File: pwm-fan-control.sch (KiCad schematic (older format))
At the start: 19 parts, among them J1 Fan-out, J2 PWM and power, J4 Fan-out, Q1 Q_PMOS_GSD, Q2 Q_PMOS_GSD, U1 LM358

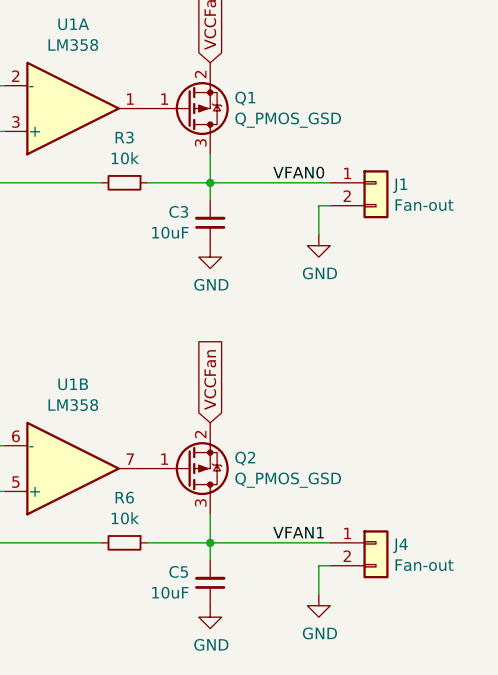
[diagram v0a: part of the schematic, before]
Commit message: improved bird, added silscreen to the back
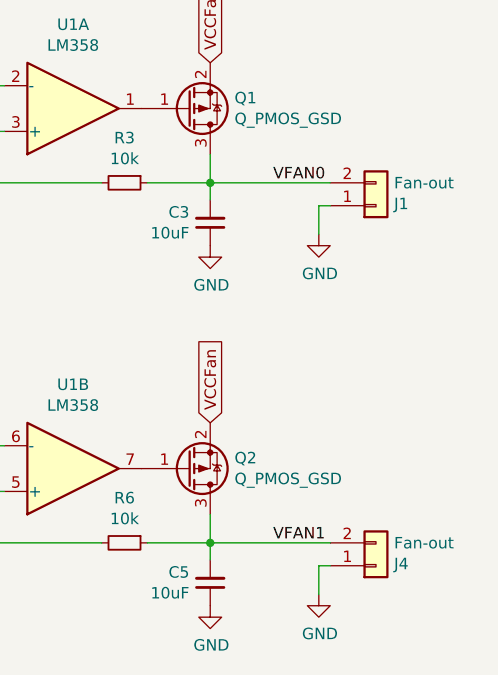
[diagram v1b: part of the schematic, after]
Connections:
- net GND: now also J1.1 (Pin_1), J4.1 (Pin_1); no longer J1.2 (Pin_2), J4.2 (Pin_2)
- net VFAN0: now also J1.2 (Pin_2); no longer J1.1 (Pin_1)
- net VFAN1: now also J4.2 (Pin_2); no longer J4.1 (Pin_1)
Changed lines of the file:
@@
 Date "2018-10-12"
 Rev "1"
-Comp "Design by N2"
+Comp "Design by N2: http://ee.david.promo"
 Comment1 "Schematic layout and PCB by Duckle"
 Comment2 ""
@@
 L Connector_Generic:Conn_01x02 J1
 U 1 1 5BC195AC
-P 6825 3775
-F 0 "J1" H 6904 3767 50  0000 L CNN
-F 1 "Fan-out" H 6904 3676 50  0000 L CNN
-F 2 "Connector_PinHeader_2.54mm:PinHeader_1x02_P2.54mm_Vertical" H 6825 3775 50  0001 C CNN
-F 3 "~" H 6825 3775 50  0001 C CNN
-	1    6825 3775
-	1    0    0    -1
+P 6825 3875
+F 0 "J1" H 6904 3867 50  0000 L CNN
+F 1 "Fan-out" H 6904 3776 50  0000 L CNN
+F 2 "Connector_PinHeader_2.54mm:PinHeader_1x02_P2.54mm_Vertical" H 6825 3875 50  0001 C CNN
+F 3 "~" H 6825 3875 50  0001 C CNN
+	1    6825 3875
+	1    0    0    1
 $EndComp
 Text Label 6375 3775 0    50   ~ 0
@@
 L Connector_Generic:Conn_01x02 J4
 U 1 1 5BC2F114
-P 6825 5350
-F 0 "J4" H 6904 5342 50  0000 L CNN
-F 1 "Fan-out" H 6904 5251 50  0000 L CNN
-F 2 "Connector_PinHeader_2.54mm:PinHeader_1x02_P2.54mm_Vertical" H 6825 5350 50  0001 C CNN
-F 3 "~" H 6825 5350 50  0001 C CNN
-	1    6825 5350
-	1    0    0    -1
+P 6825 5450
+F 0 "J4" H 6904 5442 50  0000 L CNN
+F 1 "Fan-out" H 6904 5351 50  0000 L CNN
+F 2 "Connector_PinHeader_2.54mm:PinHeader_1x02_P2.54mm_Vertical" H 6825 5450 50  0001 C CNN
+F 3 "~" H 6825 5450 50  0001 C CNN
+	1    6825 5450
+	1    0    0    1
 $EndComp
 Text Label 6375 5350 0    50   ~ 0

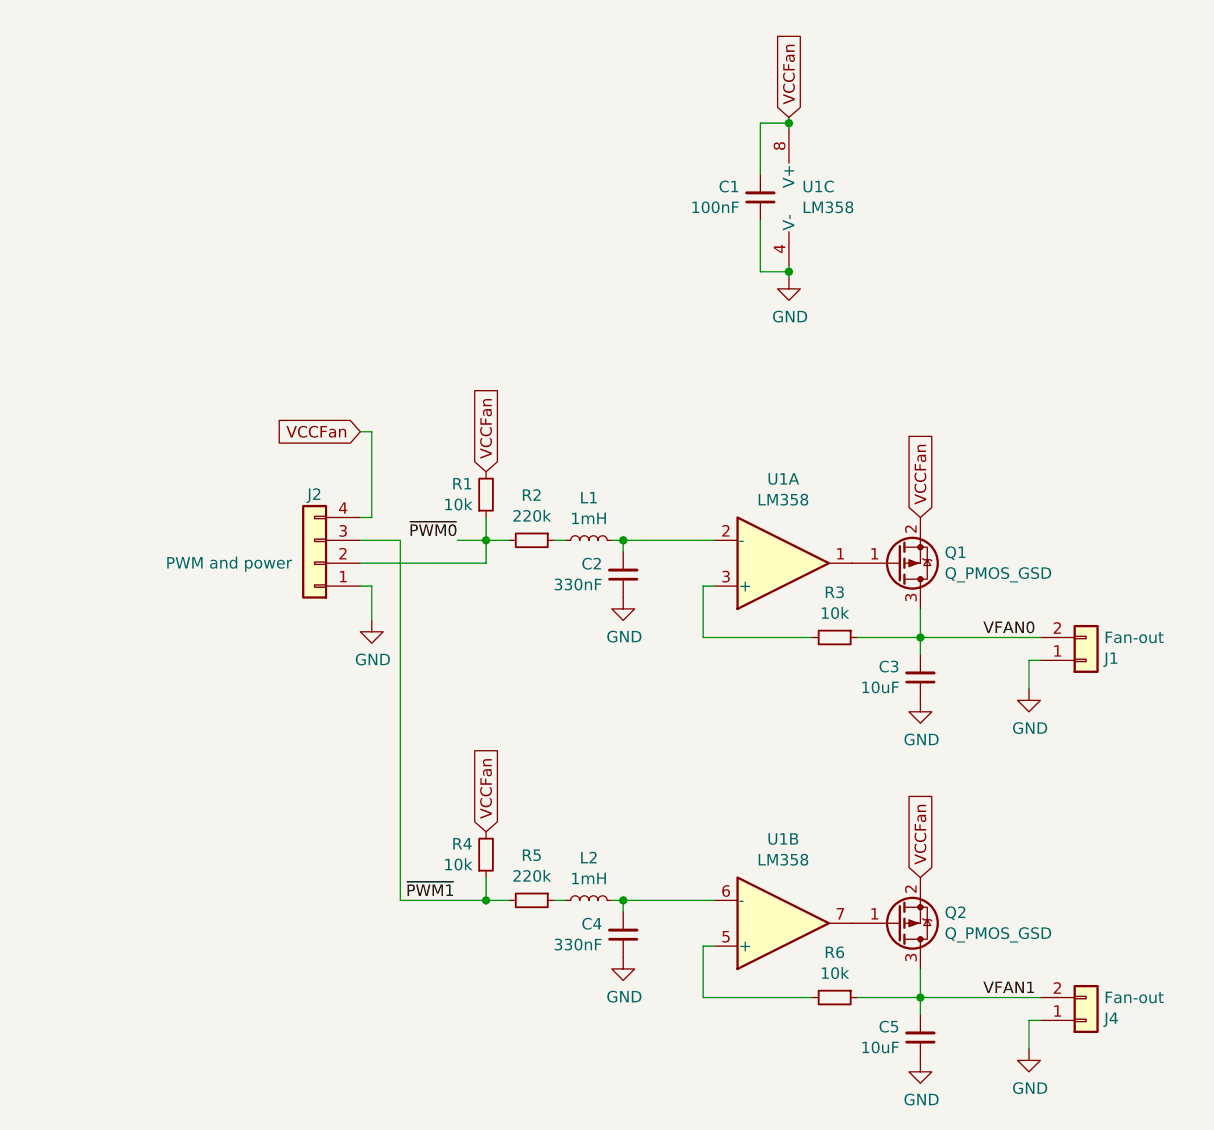
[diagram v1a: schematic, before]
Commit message: The wizard (N2) came up with a current control scheme instead
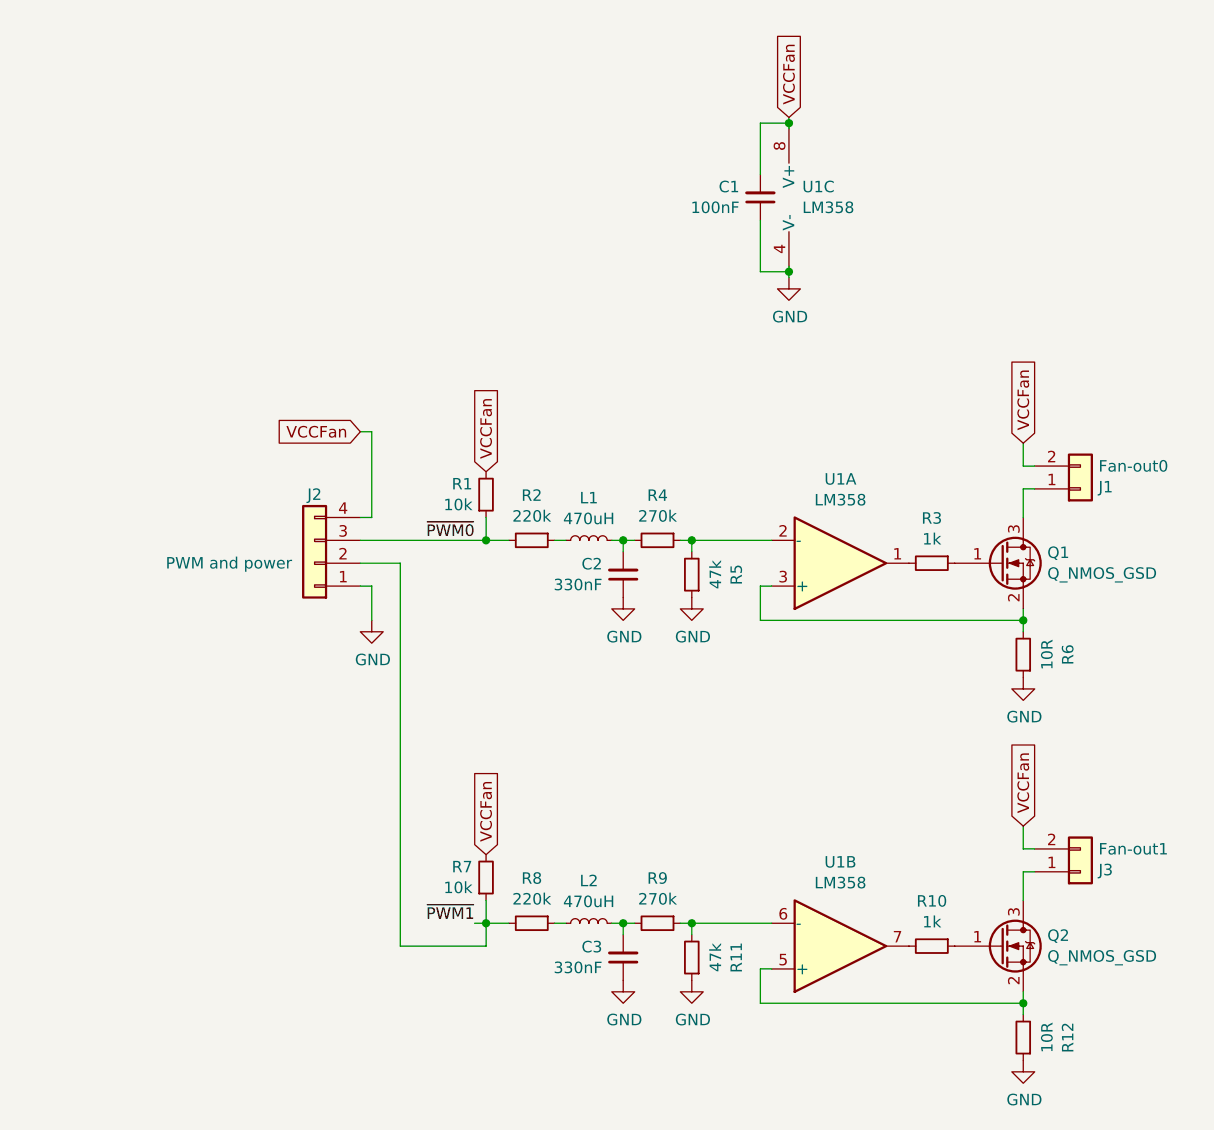
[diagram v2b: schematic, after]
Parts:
- removed C4: 330nF, Capacitor_SMD:C_0603_1608Metric_Pad1.05x0.95mm_HandSolder, symbol Device:C_Small
- removed C5: 10uF, Capacitor_SMD:CP_Elec_5x5.4, symbol Device:C_Small
- removed J4: Fan-out, Connector_PinHeader_2.54mm:PinHeader_1x02_P2.54mm_Vertical, symbol Connector_Generic:Conn_01x02
- removed Q1, Q2: Q_PMOS_GSD, Package_TO_SOT_SMD:SOT-23_Handsoldering, symbol Device:Q_PMOS_GSD
- added J3: Fan-out1, Connector:FanPinHeader_1x03_P2.54mm_Vertical, symbol Connector_Generic:Conn_01x02
- added Q1, Q2: Q_NMOS_GSD, Package_TO_SOT_SMD:TO-252-2, symbol Device:Q_NMOS_GSD
- added R10: 1k, Resistor_SMD:R_0603_1608Metric_Pad1.05x0.95mm_HandSolder, symbol Device:R_Small
- added R11: 47k, Resistor_SMD:R_0603_1608Metric_Pad1.05x0.95mm_HandSolder, symbol Device:R_Small
- added R12: 10R, Resistor_SMD:R_1206_3216Metric_Pad1.42x1.75mm_HandSolder, symbol Device:R_Small
- added R7: 10k, Resistor_SMD:R_0603_1608Metric_Pad1.05x0.95mm_HandSolder, symbol Device:R_Small
- added R8: 220k, Resistor_SMD:R_0603_1608Metric_Pad1.05x0.95mm_HandSolder, symbol Device:R_Small
- added R9: 270k, Resistor_SMD:R_0603_1608Metric_Pad1.05x0.95mm_HandSolder, symbol Device:R_Small
- C3: value 10uF -> 330nF; footprint Capacitor_SMD:CP_Elec_5x5.4 -> Capacitor_SMD:C_0603_1608Metric_Pad1.05x0.95mm_HandSolder
- J1: value Fan-out -> Fan-out0; footprint Connector_PinHeader_2.54mm:PinHeader_1x02_P2.54mm_Vertical -> Connector:FanPinHeader_1x03_P2.54mm_Vertical
- L1, L2: value 1mH -> 470uH
- R3: value 10k -> 1k
- R4: value 10k -> 270k
- R5: value 220k -> 47k
- R6: value 10k -> 10R; footprint Resistor_SMD:R_0603_1608Metric_Pad1.05x0.95mm_HandSolder -> Resistor_SMD:R_1206_3216Metric_Pad1.42x1.75mm_HandSolder
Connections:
- net VFAN1 is gone; now on net GND: R6.1
- net GND: now also R5.1, R11.1, R12.1; no longer J1.1 (Pin_1)
- net VCCFan: now also J1.2 (Pin_2), J3.2 (Pin_2), R7.2; no longer R4.2
- net ~PWM0: now also J2.3 (Pin_3); no longer J2.2 (Pin_2)
- net ~PWM1: now also J2.2 (Pin_2), R7.1, R8.2; no longer J2.3 (Pin_3), R4.1, R5.2
- net at C2.2, L1.2: now also R4.2; no longer U1.2 (-)
- net at U1.1: now also R3.2
- net at U1.3 (+): now also R6.2, Q1.2 (S); no longer R3.2
- net at L2.1: now also R8.1; no longer R5.1
- net at L2.2: now also C3.2, R9.2; no longer U1.6 (-)
- net at U1.5 (+): now also Q2.2 (S), R12.2; no longer R6.2
- net at U1.7: now also R10.2
- removed net VFAN0: C3.2, J1.2 (Pin_2), R3.1
- new net: J1.1 (Pin_1), Q1.3 (D)
- new net: R4.1, R5.2, U1.2 (-)
- new net: Q1.1 (G), R3.1
- new net: J3.1 (Pin_1), Q2.3 (D)
- new net: R11.2, R9.1, U1.6 (-)
- new net: Q2.1 (G), R10.1
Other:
- moved on the sheet: J1, R3, U1A

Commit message: Un-inverted PWM input
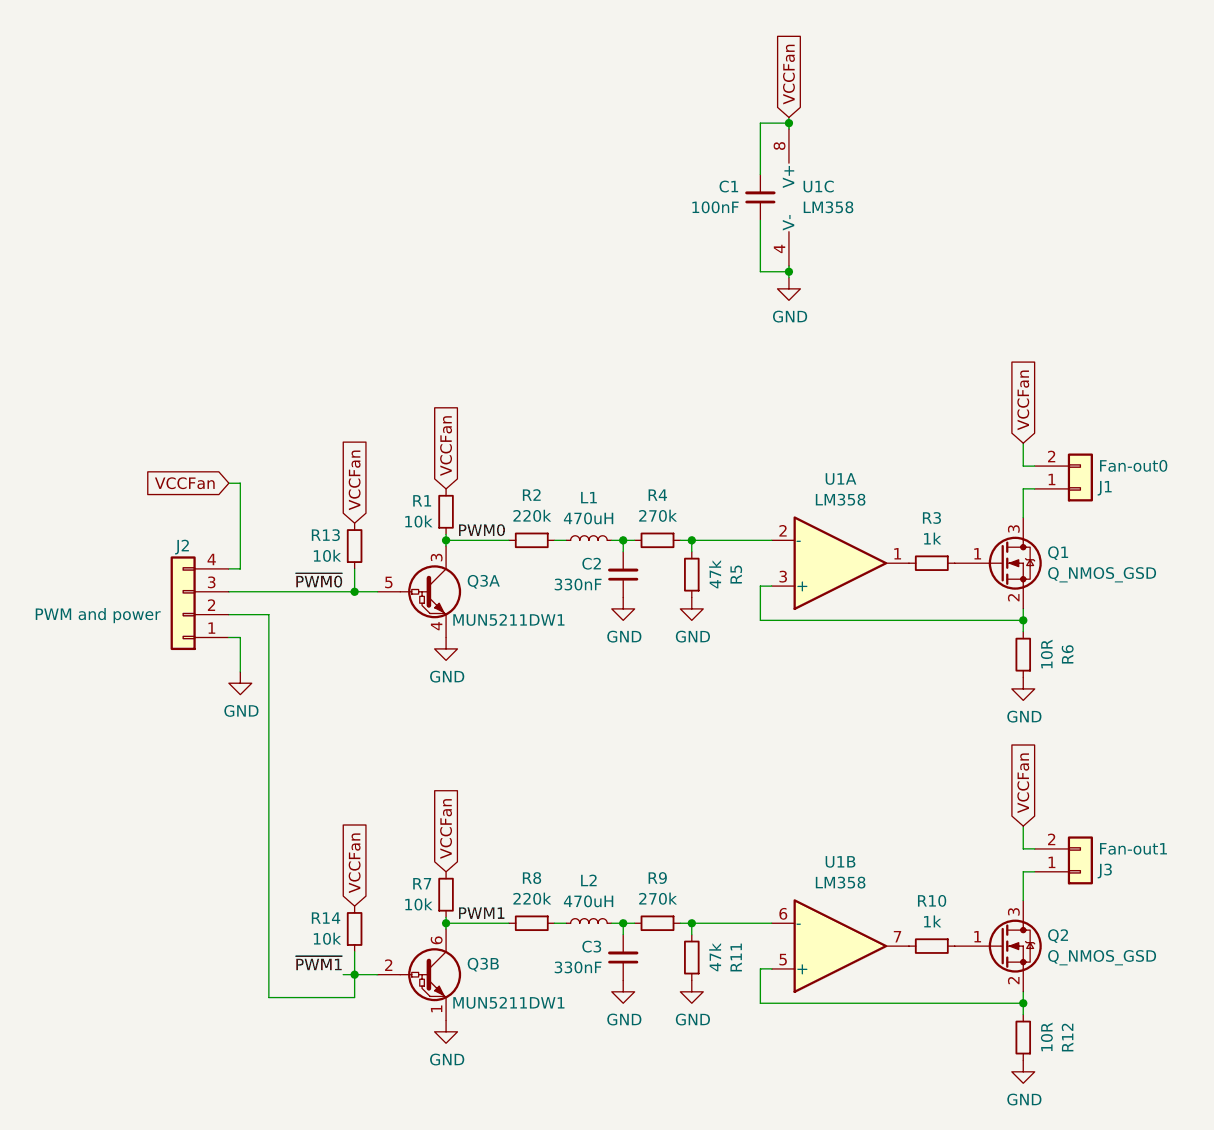
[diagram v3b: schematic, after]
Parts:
- added Q3: MUN5211DW1, Package_TO_SOT_SMD:SOT-363_SC-70-6, symbol Transistor_BJT:MUN5211DW1
- added R13, R14: 10k, Resistor_SMD:R_0603_1608Metric_Pad1.05x0.95mm_HandSolder, symbol Device:R_Small
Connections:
- net GND: now also Q3.1 (E1), Q3.4 (E1)
- net VCCFan: now also R13.2, R14.2
- net ~PWM0: now also Q3.5 (B1), R13.1; no longer R1.1, R2.2
- net ~PWM1: now also Q3.2 (B1), R14.1; no longer R7.1, R8.2
- new net PWM0: Q3.3 (C1), R1.1, R2.2
- new net PWM1: Q3.6 (C1), R7.1, R8.2
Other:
- moved on the sheet: J2, R1, R7
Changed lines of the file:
@@
 EESchema Schematic File Version 4
+LIBS:pwm-fan-control-cache
 EELAYER 26 0
 EELAYER END
@@
 	1    0    0    1
 $EndComp
-Text Label 4150 3350 2    50   ~ 0
+Text Label 3575 3575 2    50   ~ 0
 ~PWM0
-Text GLabel 3650 2875 0    50   Input ~ 0
-VCCFan
-Wire Wire Line
-	3700 2875 3650 2875
-Wire Wire Line
-	3700 3250 3700 2875
-Wire Wire Line
-	3650 3250 3700 3250
+Text GLabel 3075 3100 0    50   Input ~ 0
+VCCFan
+Wire Wire Line
+	3125 3100 3075 3100
+Wire Wire Line
+	3125 3475 3125 3100
+Wire Wire Line
+	3075 3475 3125 3475
 $Comp
 L power:GND #PWR05
 U 1 1 5BC157CF
-P 3700 3700
-F 0 "#PWR05" H 3700 3450 50  0001 C CNN
-F 1 "GND" H 3705 3527 50  0000 C CNN
-F 2 "" H 3700 3700 50  0001 C CNN
-F 3 "" H 3700 3700 50  0001 C CNN
-	1    3700 3700
-	1    0    0    -1
-$EndComp
-Wire Wire Line
-	3700 3550 3700 3700
-Wire Wire Line
-	3650 3550 3700 3550
+P 3125 3925
+F 0 "#PWR05" H 3125 3675 50  0001 C CNN
+F 1 "GND" H 3130 3752 50  0000 C CNN
+F 2 "" H 3125 3925 50  0001 C CNN
+F 3 "" H 3125 3925 50  0001 C CNN
+	1    3125 3925
+	1    0    0    -1
+$EndComp
+Wire Wire Line
+	3125 3775 3125 3925
+Wire Wire Line
+	3075 3775 3125 3775
 $Comp
 L Connector_Generic:Conn_01x04 J2
 U 1 1 5BC13D90
-P 3450 3450
-F 0 "J2" H 3450 3150 50  0000 C CNN
-F 1 "PWM and power" H 3825 3450 50  0000 C CNN
-F 2 "Connector_PinHeader_2.54mm:PinHeader_1x04_P2.54mm_Vertical" H 3450 3450 50  0001 C CNN
-F 3 "~" H 3450 3450 50  0001 C CNN
-	1    3450 3450
+P 2875 3675
+F 0 "J2" H 2875 3375 50  0000 C CNN
+F 1 "PWM and power" H 3250 3675 50  0000 C CNN
+F 2 "Connector_PinHeader_2.54mm:PinHeader_1x04_P2.54mm_Vertical" H 2875 3675 50  0001 C CNN
+F 3 "~" H 2875 3675 50  0001 C CNN
+	1    2875 3675
 	-1   0    0    1
 $EndComp
@@
 L Device:R_Small R1
 U 1 1 5BC2A6DB
-P 4200 3150
-F 0 "R1" H 4141 3104 50  0000 R CNN
-F 1 "10k" H 4141 3195 50  0000 R CNN
-F 2 "Resistor_SMD:R_0603_1608Metric_Pad1.05x0.95mm_HandSolder" H 4200 3150 50  0001 C CNN
-F 3 "~" H 4200 3150 50  0001 C CNN
-	1    4200 3150
-	1    0    0    1
-$EndComp
-Wire Wire Line
-	4200 3250 4200 3350
-Wire Wire Line
-	4200 3350 4300 3350
-Text GLabel 4200 3050 1    50   Input ~ 0
-VCCFan
-Connection ~ 4200 3350
+P 4025 3225
+F 0 "R1" H 3966 3179 50  0000 R CNN
+F 1 "10k" H 3966 3270 50  0000 R CNN
+F 2 "Resistor_SMD:R_0603_1608Metric_Pad1.05x0.95mm_HandSolder" H 4025 3225 50  0001 C CNN
+F 3 "~" H 4025 3225 50  0001 C CNN
+	1    4025 3225
+	1    0    0    1
+$EndComp
+Wire Wire Line
+	3625 3475 3625 3575
+Wire Wire Line
+	3625 3575 3725 3575
+Text GLabel 3625 3275 1    50   Input ~ 0
+VCCFan
+Connection ~ 3625 3575
 $Comp
 L Device:R_Small R4
@@
 	1    0    0    1
 $EndComp
-Text Label 4150 5025 2    50   ~ 0
+Text Label 3575 5250 2    50   ~ 0
 ~PWM1
 $Comp
@@
 L Device:R_Small R7
 U 1 1 5BC4A99C
-P 4200 4825
-F 0 "R7" H 4141 4779 50  0000 R CNN
-F 1 "10k" H 4141 4870 50  0000 R CNN
-F 2 "Resistor_SMD:R_0603_1608Metric_Pad1.05x0.95mm_HandSolder" H 4200 4825 50  0001 C CNN
-F 3 "~" H 4200 4825 50  0001 C CNN
-	1    4200 4825
-	1    0    0    1
-$EndComp
-Wire Wire Line
-	4200 4925 4200 5025
-Wire Wire Line
-	4200 5025 4300 5025
-Text GLabel 4200 4725 1    50   Input ~ 0
-VCCFan
-Wire Wire Line
-	4150 5025 4200 5025
-Connection ~ 4200 5025
-Wire Wire Line
-	4200 5125 4200 5025
+P 4025 4900
+F 0 "R7" H 3966 4854 50  0000 R CNN
+F 1 "10k" H 3966 4945 50  0000 R CNN
+F 2 "Resistor_SMD:R_0603_1608Metric_Pad1.05x0.95mm_HandSolder" H 4025 4900 50  0001 C CNN
+F 3 "~" H 4025 4900 50  0001 C CNN
+	1    4025 4900
+	1    0    0    1
+$EndComp
+Wire Wire Line
+	3625 5150 3625 5250
+Wire Wire Line
+	3625 5250 3725 5250
+Text GLabel 3625 4950 1    50   Input ~ 0
+VCCFan
+Wire Wire Line
+	3575 5250 3625 5250
+Connection ~ 3625 5250
+Wire Wire Line
+	3625 5350 3625 5250
 $Comp
 L Device:R_Small R9
@@
 	6550 5375 6550 5425
 Wire Wire Line
-	3825 5125 4200 5125
-Wire Wire Line
-	3650 3350 4200 3350
-Wire Wire Line
-	3825 5125 3825 3450
-Wire Wire Line
-	3825 3450 3650 3450
+	3250 5350 3625 5350
+Wire Wire Line
+	3075 3575 3625 3575
+Wire Wire Line
+	3250 5350 3250 3675
+Wire Wire Line
+	3250 3675 3075 3675
+$Comp
+L Transistor_BJT:MUN5211DW1 Q3
+U 1 1 5BC58726
+P 3975 3575
+F 0 "Q3" H 4116 3621 50  0000 L CNN
+F 1 "MUN5211DW1" H 4050 3450 50  0000 L CNN
+F 2 "Package_TO_SOT_SMD:SOT-363_SC-70-6" H 3980 3135 50  0001 C CNN
+F 3 "http://www.onsemi.com/pub/Collateral/DTC114ED-D.PDF" H 3975 3575 50  0001 C CNN
+	1    3975 3575
+	1    0    0    -1
+$EndComp
+$Comp
+L power:GND #PWR0105
+U 1 1 5BC58BCA
+P 4025 3775
+F 0 "#PWR0105" H 4025 3525 50  0001 C CNN
+F 1 "GND" H 4030 3602 50  0000 C CNN
+F 2 "" H 4025 3775 50  0001 C CNN
+F 3 "" H 4025 3775 50  0001 C CNN
+	1    4025 3775
+	1    0    0    -1
+$EndComp
+$Comp
+L Device:R_Small R13
+U 1 1 5BC5C8A0
+P 3625 3375
+F 0 "R13" H 3566 3329 50  0000 R CNN
+F 1 "10k" H 3566 3420 50  0000 R CNN
+F 2 "Resistor_SMD:R_0603_1608Metric_Pad1.05x0.95mm_HandSolder" H 3625 3375 50  0001 C CNN
+F 3 "~" H 3625 3375 50  0001 C CNN
+	1    3625 3375
+	1    0    0    1
+$EndComp
+Text GLabel 4025 3125 1    50   Input ~ 0
+VCCFan
+Wire Wire Line
+	4025 3325 4025 3350
+Wire Wire Line
+	4025 3350 4300 3350
+Connection ~ 4025 3350
+Wire Wire Line
+	4025 3350 4025 3375
+$Comp
+L Transistor_BJT:MUN5211DW1 Q3
+U 2 1 5BC60353
+P 3975 5250
+F 0 "Q3" H 4116 5296 50  0000 L CNN
+F 1 "MUN5211DW1" H 4050 5125 50  0000 L CNN
+F 2 "Package_TO_SOT_SMD:SOT-363_SC-70-6" H 3980 4810 50  0001 C CNN
+F 3 "http://www.onsemi.com/pub/Collateral/DTC114ED-D.PDF" H 3975 5250 50  0001 C CNN
+	2    3975 5250
+	1    0    0    -1
+$EndComp
+$Comp
+L power:GND #PWR0106
+U 1 1 5BC60359
+P 4025 5450
+F 0 "#PWR0106" H 4025 5200 50  0001 C CNN
+F 1 "GND" H 4030 5277 50  0000 C CNN
+F 2 "" H 4025 5450 50  0001 C CNN
+F 3 "" H 4025 5450 50  0001 C CNN
+	1    4025 5450
+	1    0    0    -1
+$EndComp
+$Comp
+L Device:R_Small R14
+U 1 1 5BC6035F
+P 3625 5050
+F 0 "R14" H 3566 5004 50  0000 R CNN
+F 1 "10k" H 3566 5095 50  0000 R CNN
+F 2 "Resistor_SMD:R_0603_1608Metric_Pad1.05x0.95mm_HandSolder" H 3625 5050 50  0001 C CNN
+F 3 "~" H 3625 5050 50  0001 C CNN
+	1    3625 5050
+	1    0    0    1
+$EndComp
+Text GLabel 4025 4800 1    50   Input ~ 0
+VCCFan
+Wire Wire Line
+	4025 5000 4025 5025
+Wire Wire Line
+	4025 5025 4300 5025
+Connection ~ 4025 5025
+Wire Wire Line
+	4025 5025 4025 5050
+Text Label 4075 3350 0    50   ~ 0
+PWM0
+Text Label 4075 5025 0    50   ~ 0
+PWM1
 $EndSCHEMATC
